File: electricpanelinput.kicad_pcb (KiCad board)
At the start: 2 copper layers, 86.4 x 44.4 mm, 25 parts, among them J1 5V, J10 Blu-, J11 Blu+, J12 Vic-, J13 Vic+, J2 12V, J3 VDC, J4 GND, J5 CRE, J6 BlueSun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

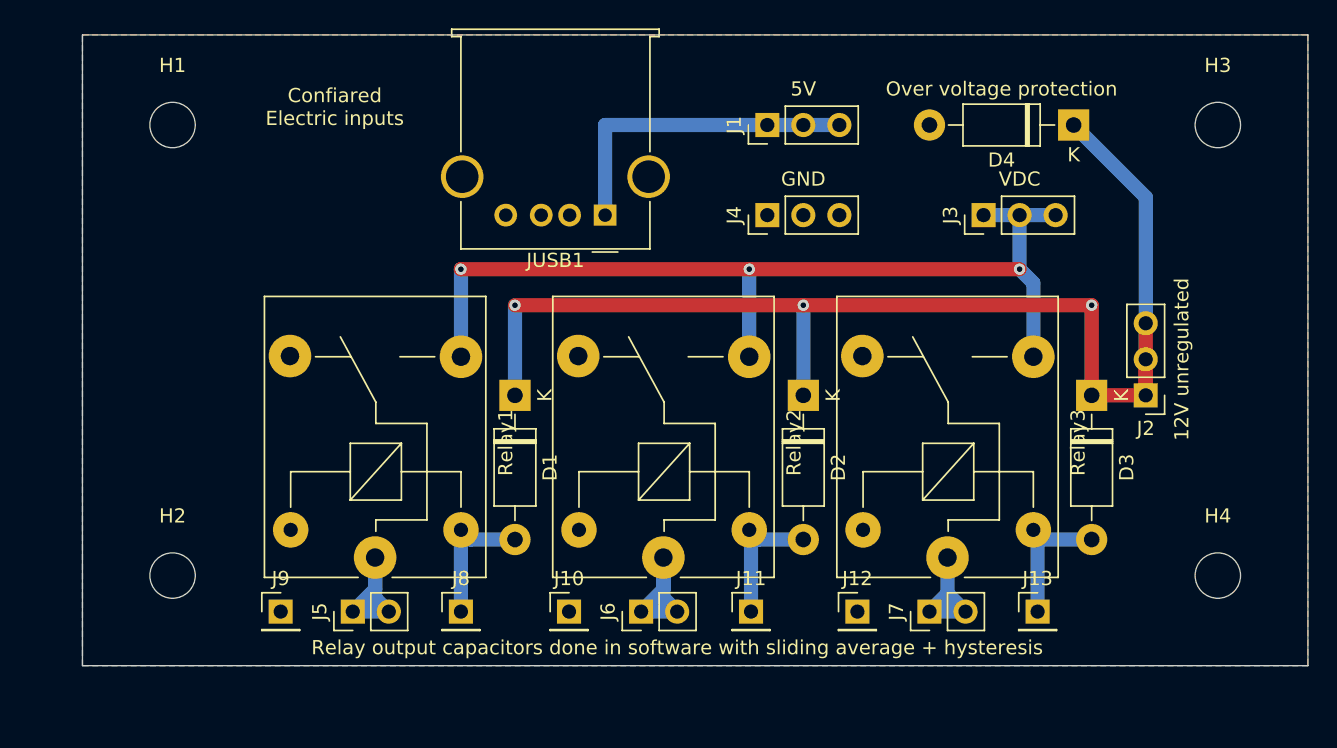
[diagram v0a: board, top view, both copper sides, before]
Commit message: 1 Layer PCB, input resistor protection
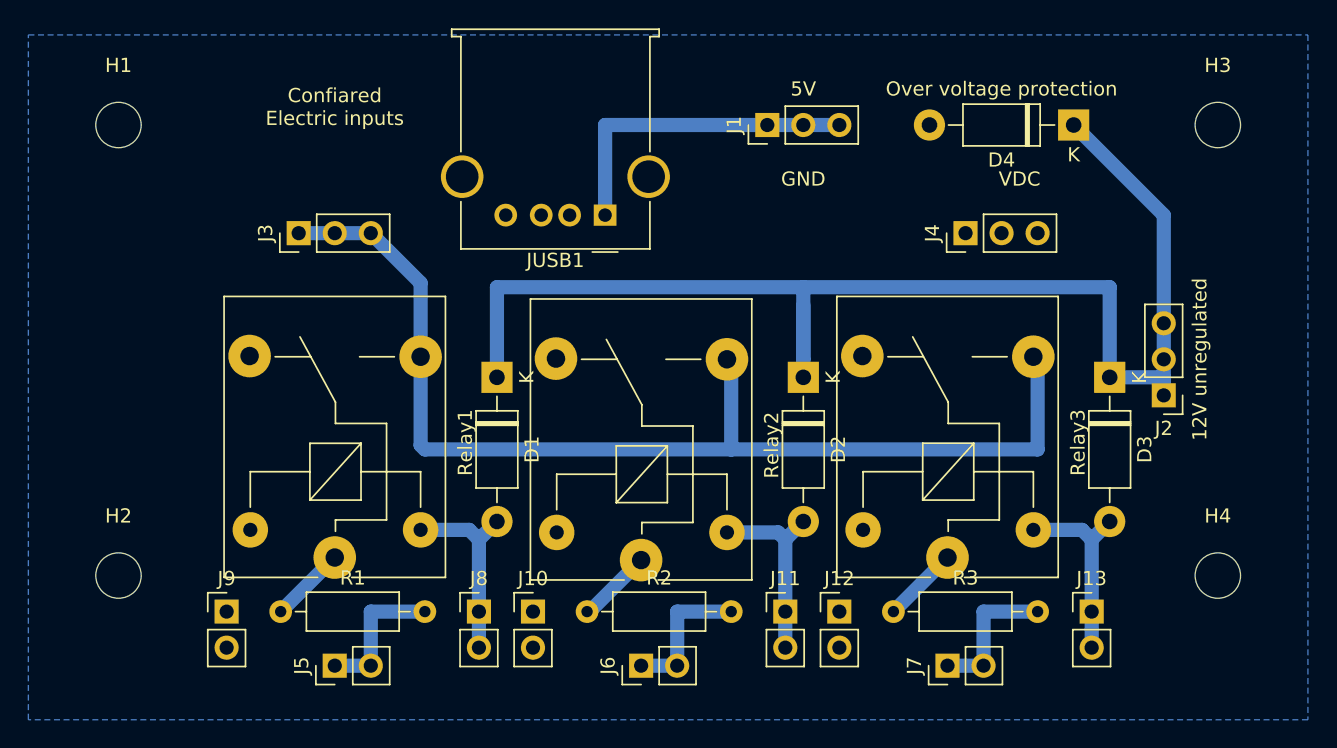
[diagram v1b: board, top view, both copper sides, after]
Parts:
- added R1: 1k, Resistor_THT:R_Axial_DIN0207_L6.3mm_D2.5mm_P10.16mm_Horizontal, F.Cu at (121.9, 157.5)
- added R2: 1k, Resistor_THT:R_Axial_DIN0207_L6.3mm_D2.5mm_P10.16mm_Horizontal, F.Cu at (143.5, 157.5)
- added R3: 1k, Resistor_THT:R_Axial_DIN0207_L6.3mm_D2.5mm_P10.16mm_Horizontal, F.Cu at (165.1, 157.5)
- J10, J11, J12, J13, J8, J9: footprint Connector_PinHeader_2.54mm:PinHeader_1x01_P2.54mm_Vertical -> Connector_PinHeader_2.54mm:PinHeader_1x02_P2.54mm_Vertical
- moved J3 48.3 mm to (123.2, 130.8)
- moved J4 14.0 mm to (170.2, 130.8)
- moved J7 4.02 mm to (168.9, 161.3)
- moved J5 4.02 mm to (125.7, 161.3)
- moved H1 3.81 mm to (110.5, 123.2)
- moved H2 3.81 mm to (110.5, 154.9)
- moved J13 3.81 mm to (179.1, 157.5)
- moved J6 3.81 mm to (147.3, 161.3)
- moved J9 3.81 mm to (118.1, 157.5)
- moved Relay1 2.85 mm to (125.7, 153.7)
- moved J10 2.54 mm to (139.7, 157.5)
- moved J11 2.41 mm to (157.5, 157.5)
- moved D1 1.80 mm to (137.2, 141.0)
- moved D3 1.80 mm to (180.3, 141.0)
- moved Relay2 1.58 mm to (147.3, 153.8)
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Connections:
- Relay1 pad 1: /OCRE -> Net-(R1-Pad1)
- Relay2 pad 1: /OBlu -> Net-(R2-Pad1)
- Relay3 pad 1: /OVic -> Net-(R3-Pad1)
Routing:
- net /VDC: track 67.2 -> 78.6 mm, vias 3 -> 0
- net /12Vunregulated: track 98.6 -> 92.8 mm, vias 3 -> 0
- net Net-(R3-Pad1): track 0.00 -> 5.39 mm
- net Net-(R1-Pad1): track 0.00 -> 5.39 mm
- net Net-(R2-Pad1): track 0.00 -> 5.31 mm
- net /CRE+: track 9.85 -> 13.8 mm
- net /Blu+: track 9.90 -> 13.7 mm
- net /Vic+: track 10.3 -> 13.8 mm
- net /OVic: track 8.67 -> 10.2 mm
- net /OBlu: track 11.2 -> 10.2 mm
- net /OCRE: track 11.2 -> 10.2 mm
- removed copper zone on F.Cu, net 0
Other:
- board outline removed
- board text removed: "Relay output capacitors done in software with sliding average + hysteresis"
